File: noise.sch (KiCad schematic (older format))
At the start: 38 parts, among them J10 noisepresel, J11 noisein-pre, J12 noiseoutsrc, J7 noisesel, J8 noisein, J9 noiseout, U1 4584, U2 TL074, U3 78L05

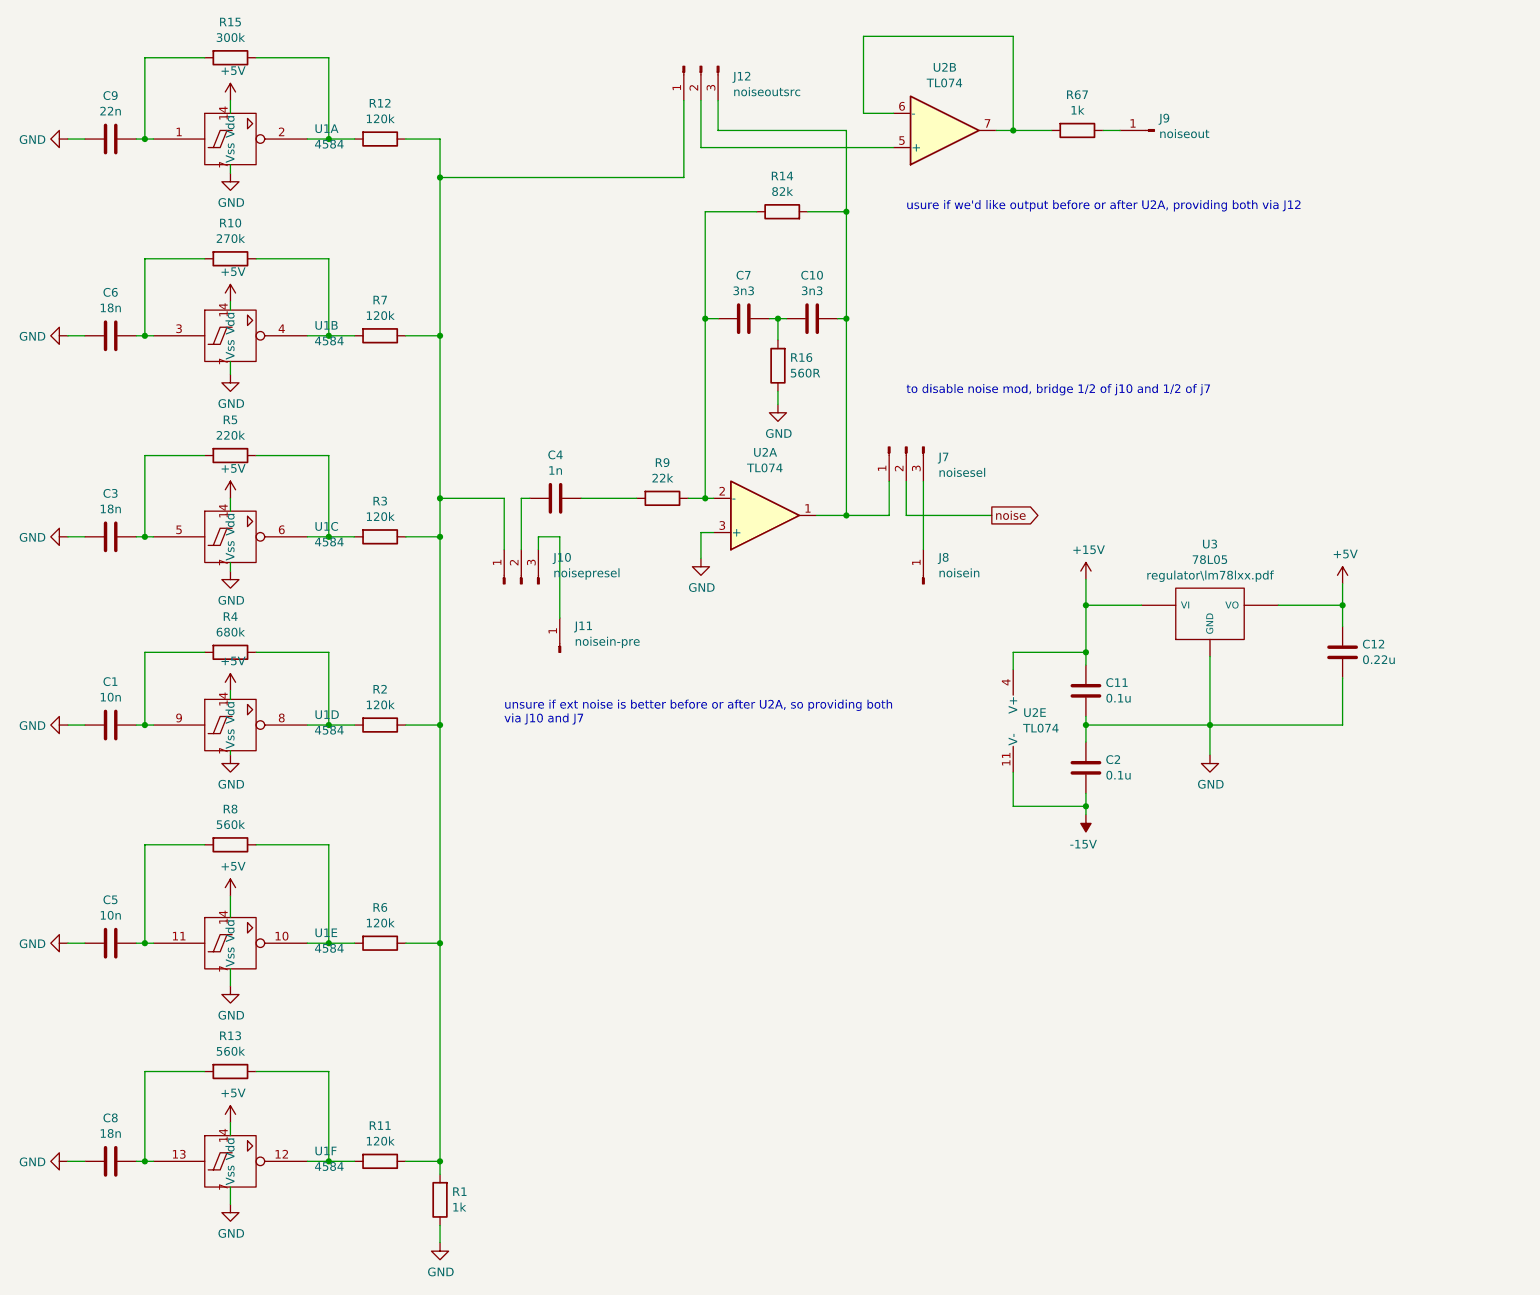
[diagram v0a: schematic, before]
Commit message: selected some parts
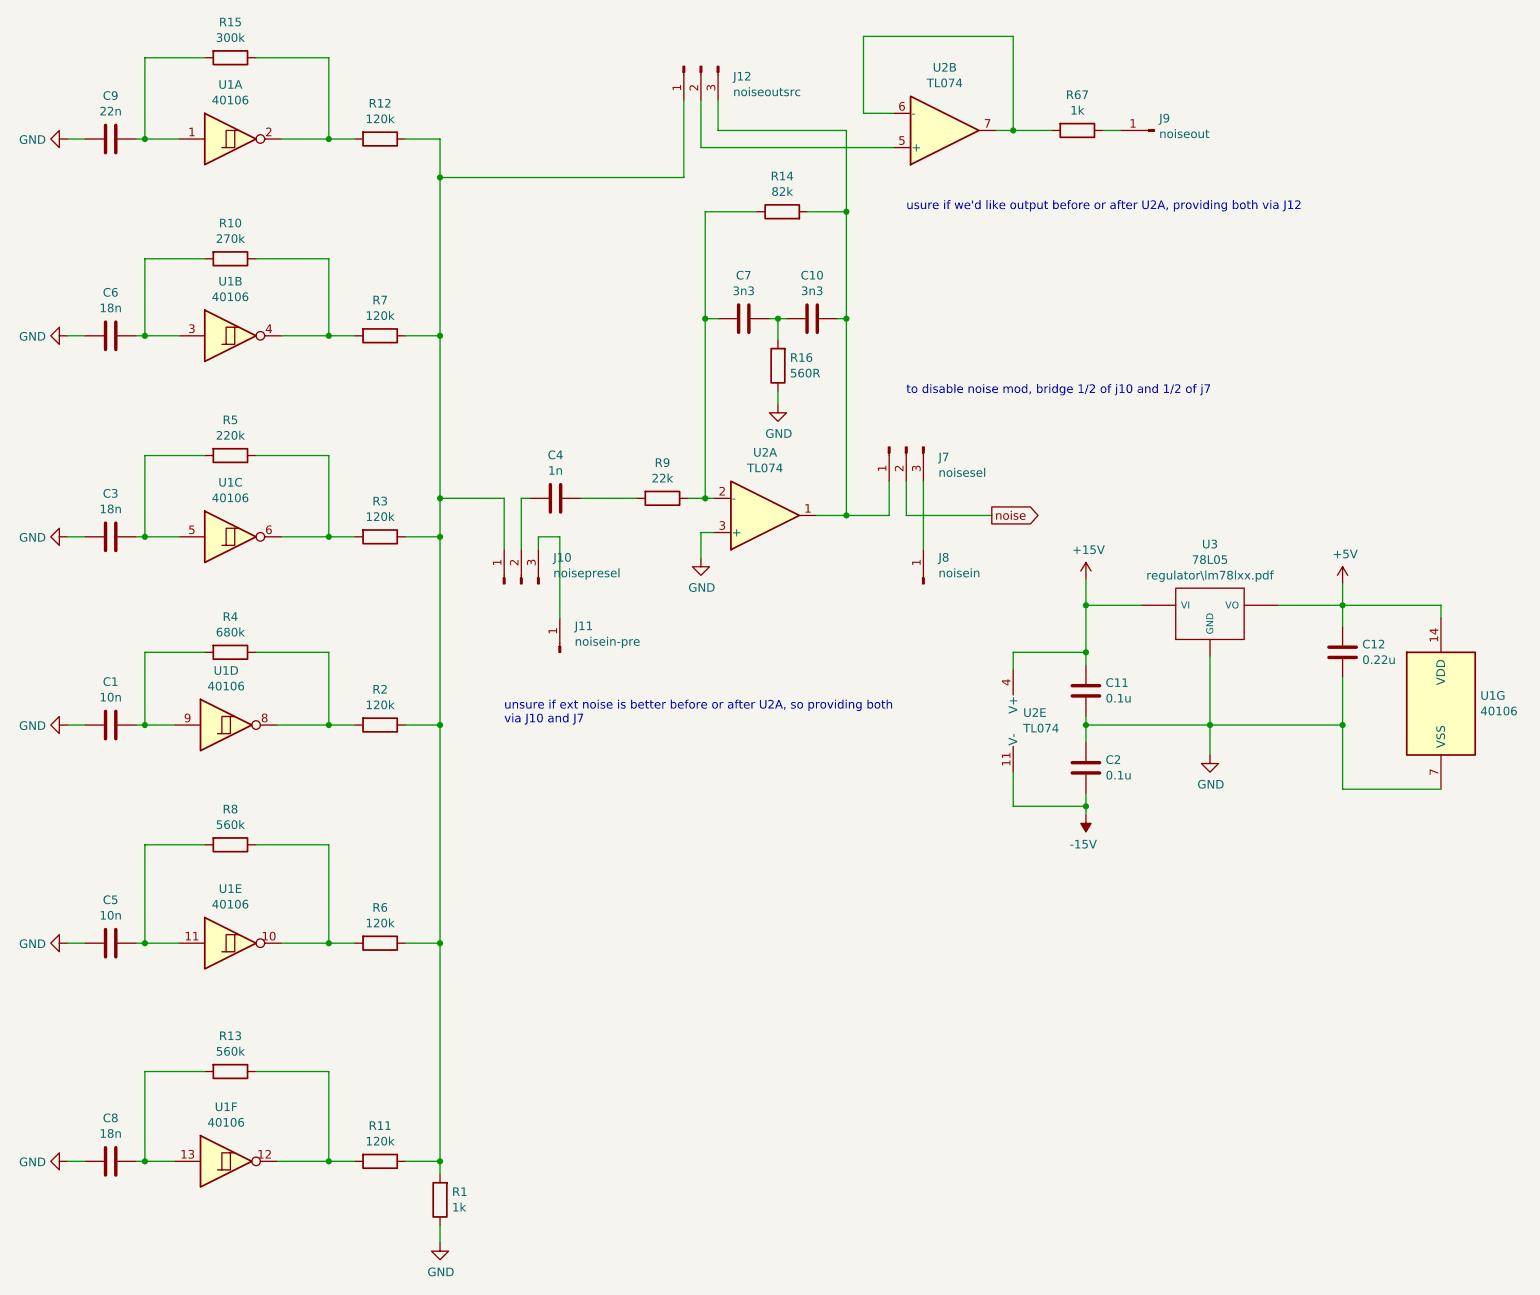
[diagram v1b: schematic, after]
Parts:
- removed U1: 4584, symbol 4xxx_IEEE:4584
- added U1: 40106, Package_DIP:DIP-14_W7.62mm_LongPads, symbol 4xxx:40106
- J10, J12, J7: footprint (none) -> Connector_PinHeader_2.54mm:PinHeader_1x03_P2.54mm_Vertical
- J11, J8, J9: footprint (none) -> Connector_PinHeader_2.54mm:PinHeader_1x01_P2.54mm_Vertical
- R1, R10, R11, R12, R13, R14, R15, R16, R2, R3, R4, R5, R6, R67, R7, R8, R9: footprint (none) -> Resistor_THT:R_Axial_DIN0204_L3.6mm_D1.6mm_P7.62mm_Horizontal
- U2: footprint (none) -> Package_DIP:DIP-14_W7.62mm_LongPads
- U3: footprint (none) -> Package_TO_SOT_THT:TO-220-3_Vertical
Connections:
- net +5V: now also U1.14 (VDD)
- net GND: now also U1.7 (VSS)
- net at C9.1, R15.2: now also U1.1
- net at R12.2, R15.1: now also U1.2
- net at C6.1, R10.2: now also U1.3
- net at R10.1, R7.2: now also U1.4
- net at C3.1, R5.2: now also U1.5
- net at R3.2, R5.1: now also U1.6
- net at R2.2, R4.1: now also U1.8
- net at C1.1, R4.2: now also U1.9
- net at R6.2, R8.1: now also U1.10
- net at C5.1, R8.2: now also U1.11
- net at R11.2, R13.1: now also U1.12
- net at C8.1, R13.2: now also U1.13

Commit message: assigned footprints
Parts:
- C1, C10, C11, C12, C2, C3, C4, C5, C6, C7, C8: footprint (none) -> Capacitor_THT:C_Disc_D3.4mm_W2.1mm_P2.50mm
- C9: footprint (none) -> Capacitor_THT:C_Disc_D4.3mm_W1.9mm_P5.00mm
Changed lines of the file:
@@
 F 0 "C9" V 773 1200 50  0000 C CNN
 F 1 "22n" V 864 1200 50  0000 C CNN
-F 2 "" H 1063 1050 50  0001 C CNN
+F 2 "Capacitor_THT:C_Disc_D4.3mm_W1.9mm_P5.00mm" H 1063 1050 50  0001 C CNN
 F 3 "~" H 1025 1200 50  0001 C CNN
 	1    1025 1200
@@
 F 0 "C6" V 773 2350 50  0000 C CNN
 F 1 "18n" V 864 2350 50  0000 C CNN
-F 2 "" H 1063 2200 50  0001 C CNN
+F 2 "Capacitor_THT:C_Disc_D3.4mm_W2.1mm_P2.50mm" H 1063 2200 50  0001 C CNN
 F 3 "~" H 1025 2350 50  0001 C CNN
 	1    1025 2350
@@
 F 0 "C3" V 773 3525 50  0000 C CNN
 F 1 "18n" V 864 3525 50  0000 C CNN
-F 2 "" H 1063 3375 50  0001 C CNN
+F 2 "Capacitor_THT:C_Disc_D3.4mm_W2.1mm_P2.50mm" H 1063 3375 50  0001 C CNN
 F 3 "~" H 1025 3525 50  0001 C CNN
 	1    1025 3525
@@
 F 0 "C1" V 773 4625 50  0000 C CNN
 F 1 "10n" V 864 4625 50  0000 C CNN
-F 2 "" H 1063 4475 50  0001 C CNN
+F 2 "Capacitor_THT:C_Disc_D3.4mm_W2.1mm_P2.50mm" H 1063 4475 50  0001 C CNN
 F 3 "~" H 1025 4625 50  0001 C CNN
 	1    1025 4625
@@
 F 0 "C5" V 773 5900 50  0000 C CNN
 F 1 "10n" V 864 5900 50  0000 C CNN
-F 2 "" H 1063 5750 50  0001 C CNN
+F 2 "Capacitor_THT:C_Disc_D3.4mm_W2.1mm_P2.50mm" H 1063 5750 50  0001 C CNN
 F 3 "~" H 1025 5900 50  0001 C CNN
 	1    1025 5900
@@
 F 0 "C8" V 773 7175 50  0000 C CNN
 F 1 "18n" V 864 7175 50  0000 C CNN
-F 2 "" H 1063 7025 50  0001 C CNN
+F 2 "Capacitor_THT:C_Disc_D3.4mm_W2.1mm_P2.50mm" H 1063 7025 50  0001 C CNN
 F 3 "~" H 1025 7175 50  0001 C CNN
 	1    1025 7175
@@
 F 0 "C4" V 3373 3300 50  0000 C CNN
 F 1 "1n" V 3464 3300 50  0000 C CNN
-F 2 "" H 3663 3150 50  0001 C CNN
+F 2 "Capacitor_THT:C_Disc_D3.4mm_W2.1mm_P2.50mm" H 3663 3150 50  0001 C CNN
 F 3 "~" H 3625 3300 50  0001 C CNN
 	1    3625 3300
@@
 F 0 "C7" V 4473 2250 50  0000 C CNN
 F 1 "3n3" V 4564 2250 50  0000 C CNN
-F 2 "" H 4763 2100 50  0001 C CNN
+F 2 "Capacitor_THT:C_Disc_D3.4mm_W2.1mm_P2.50mm" H 4763 2100 50  0001 C CNN
 F 3 "~" H 4725 2250 50  0001 C CNN
 	1    4725 2250
@@
 F 0 "C10" V 4873 2250 50  0000 C CNN
 F 1 "3n3" V 4964 2250 50  0000 C CNN
-F 2 "" H 5163 2100 50  0001 C CNN
+F 2 "Capacitor_THT:C_Disc_D3.4mm_W2.1mm_P2.50mm" H 5163 2100 50  0001 C CNN
 F 3 "~" H 5125 2250 50  0001 C CNN
 	1    5125 2250
@@
 F 0 "C11" H 6840 4471 50  0000 L CNN
 F 1 "0.1u" H 6840 4380 50  0000 L CNN
-F 2 "" H 6763 4275 50  0001 C CNN
+F 2 "Capacitor_THT:C_Disc_D3.4mm_W2.1mm_P2.50mm" H 6763 4275 50  0001 C CNN
 F 3 "~" H 6725 4425 50  0001 C CNN
 	1    6725 4425
@@
 F 0 "C2" H 6840 4921 50  0000 L CNN
 F 1 "0.1u" H 6840 4830 50  0000 L CNN
-F 2 "" H 6763 4725 50  0001 C CNN
+F 2 "Capacitor_THT:C_Disc_D3.4mm_W2.1mm_P2.50mm" H 6763 4725 50  0001 C CNN
 F 3 "~" H 6725 4875 50  0001 C CNN
 	1    6725 4875
@@
 F 0 "C12" H 8340 4246 50  0000 L CNN
 F 1 "0.22u" H 8340 4155 50  0000 L CNN
-F 2 "" H 8263 4050 50  0001 C CNN
+F 2 "Capacitor_THT:C_Disc_D3.4mm_W2.1mm_P2.50mm" H 8263 4050 50  0001 C CNN
 F 3 "~" H 8225 4200 50  0001 C CNN
 	1    8225 4200
